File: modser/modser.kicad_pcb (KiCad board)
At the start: 2 copper layers, 32 x 32 mm, 21 parts, among them IC1 AS5600-ASOT, J1 Conn_01x03_Socket, J3 Conn_01x02_Socket, U1 DRV8313PWPR, U2 XIAO-RP2040-DIP, U3 AP63203WU-7

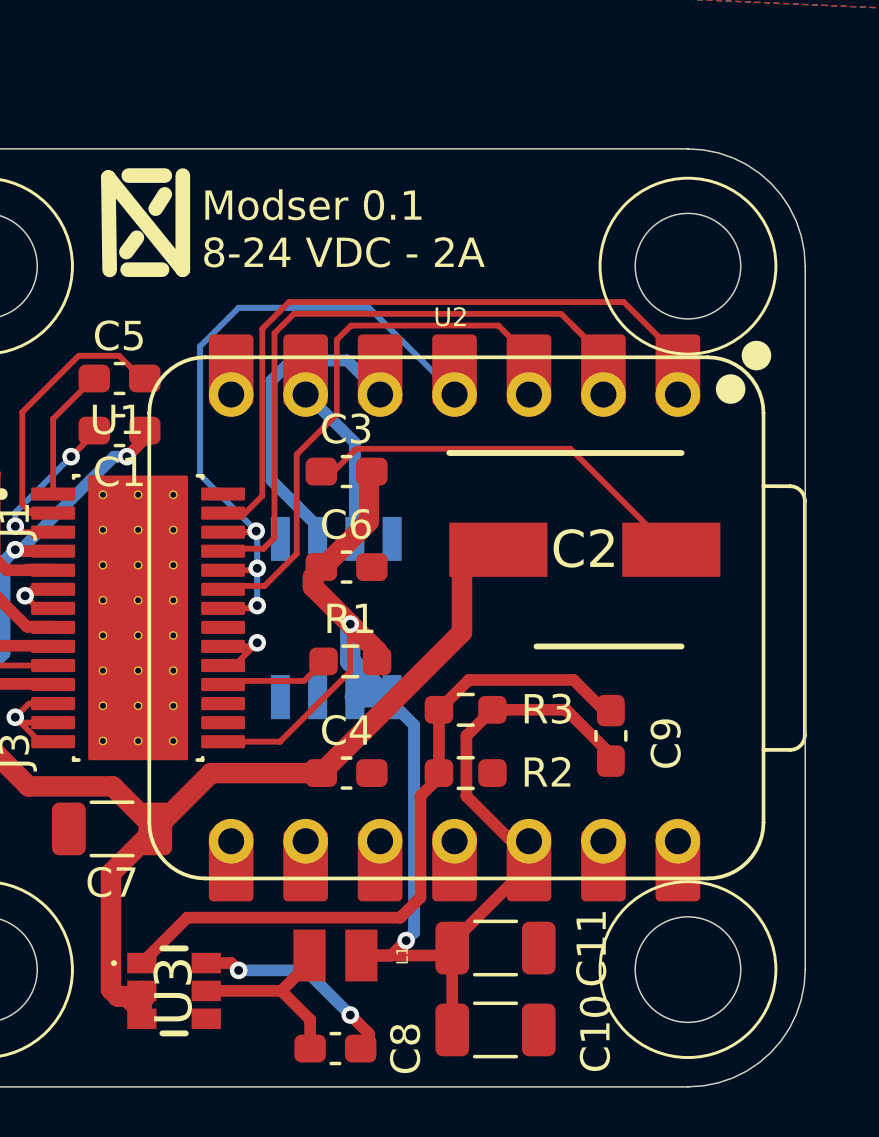
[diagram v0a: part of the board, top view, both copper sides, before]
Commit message: Fixed issue with design around power regulator
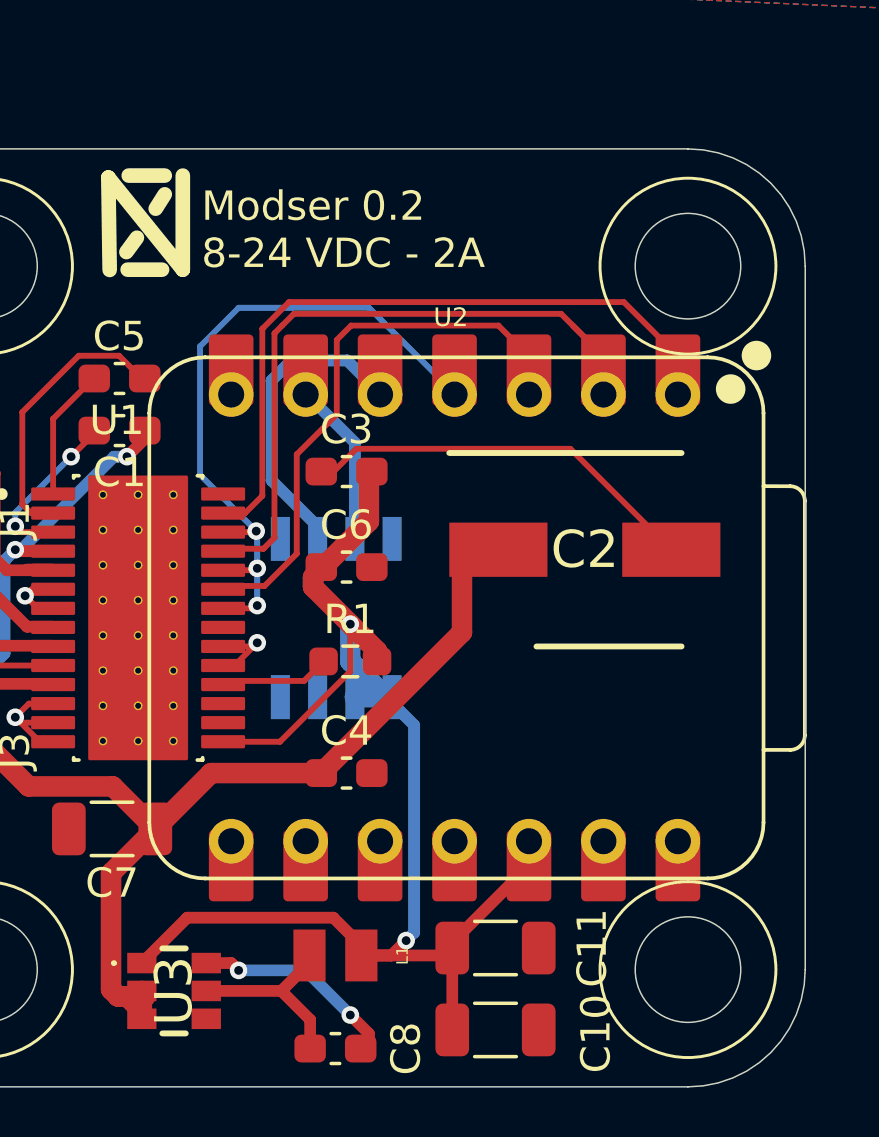
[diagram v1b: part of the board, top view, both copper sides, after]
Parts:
- removed C9: 100 pF, Capacitor_SMD:C_0603_1608Metric_Pad1.08x0.95mm_HandSolder
- removed R2: 30.9 kOhm, Resistor_SMD:R_0603_1608Metric_Pad0.98x0.95mm_HandSolder
- removed R3: 62 kOhm, Resistor_SMD:R_0603_1608Metric_Pad0.98x0.95mm_HandSolder
- L1: value 2.2 uH -> 3.9 uH
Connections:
- U3 pad 1: RegFB -> +3.3V
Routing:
- net RegFB: track 24.0 -> 0.00 mm
- net +3.3V: track 51.2 -> 48.7 mm
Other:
- board text added: "Modser 0.2 8-24 VDC - 2A"
- board text removed: "Modser 0.1 8-24 VDC - 2A"

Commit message: Fixed issue where reset and sleep lines were never pulled high as required
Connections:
- U1 pad 16: unconnected-(U1-~{RESET}-Pad16) -> Enable
- U1 pad 17: unconnected-(U1-~{SLEEP}-Pad17) -> Enable
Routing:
- net Enable: track 23.1 -> 27.6 mm, vias 3 -> 4
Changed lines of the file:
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@@
 	(net 18 "Enable")
 	(net 19 "Net-(U1-IN1)")
-	(net 20 "unconnected-(U1-~{SLEEP}-Pad17)")
-	(net 21 "unconnected-(U1-NC-Pad21)")
-	(net 22 "Net-(U1-IN2)")
-	(net 23 "unconnected-(U1-~{RESET}-Pad16)")
-	(net 24 "unconnected-(U1-EXP-Pad29)")
-	(net 25 "unconnected-(U2-GPIO1{slash}RX-Pad8)")
-	(net 26 "unconnected-(U2-GPIO0{slash}TX-Pad7)")
-	(net 27 "unconnected-(U2-GPIO2{slash}SCK-Pad9)")
-	(net 28 "unconnected-(U2-VBUS-Pad14)")
-	(net 29 "unconnected-(U2-GPIO2{slash}SCK-Pad9)_1")
-	(net 30 "unconnected-(U2-GPIO3{slash}MOSI-Pad11)")
-	(net 31 "unconnected-(U2-GPIO4{slash}MISO-Pad10)")
-	(net 32 "unconnected-(U2-GPIO3{slash}MOSI-Pad11)_1")
-	(net 33 "unconnected-(U2-VBUS-Pad14)_1")
-	(net 34 "unconnected-(U2-GPIO4{slash}MISO-Pad10)_1")
-	(net 35 "unconnected-(U2-GPIO1{slash}RX-Pad8)_1")
-	(net 36 "unconnected-(U2-GPIO0{slash}TX-Pad7)_1")
+	(net 20 "unconnected-(U1-NC-Pad21)")
+	(net 21 "Net-(U1-IN2)")
+	(net 22 "unconnected-(U1-EXP-Pad29)")
+	(net 23 "unconnected-(U2-GPIO1{slash}RX-Pad8)")
+	(net 24 "unconnected-(U2-GPIO0{slash}TX-Pad7)")
+	(net 25 "unconnected-(U2-GPIO2{slash}SCK-Pad9)")
+	(net 26 "unconnected-(U2-VBUS-Pad14)")
+	(net 27 "unconnected-(U2-GPIO2{slash}SCK-Pad9)_1")
+	(net 28 "unconnected-(U2-GPIO3{slash}MOSI-Pad11)")
+	(net 29 "unconnected-(U2-GPIO4{slash}MISO-Pad10)")
+	(net 30 "unconnected-(U2-GPIO3{slash}MOSI-Pad11)_1")
+	(net 31 "unconnected-(U2-VBUS-Pad14)_1")
+	(net 32 "unconnected-(U2-GPIO4{slash}MISO-Pad10)_1")
+	(net 33 "unconnected-(U2-GPIO1{slash}RX-Pad8)_1")
+	(net 34 "unconnected-(U2-GPIO0{slash}TX-Pad7)_1")
 	(footprint "Capacitor_SMD:C_1206_3216Metric"
 		(layer "F.Cu")
@@
 			(layers "F.Cu" "F.Mask")
 			(roundrect_rratio 0.1)
-			(net 22 "Net-(U1-IN2)")
+			(net 21 "Net-(U1-IN2)")
 			(pinfunction "GPIO27/ADC1/A1")
 			(pintype "passive")
@@
 			(layers "*.Cu" "*.Mask")
 			(remove_unused_layers no)
-			(net 22 "Net-(U1-IN2)")
+			(net 21 "Net-(U1-IN2)")
 			(pinfunction "GPIO27/ADC1/A1")
 			(pintype "passive")
@@
 			(layers "F.Cu" "F.Mask")
 			(roundrect_rratio 0.1)
-			(net 36 "unconnected-(U2-GPIO0{slash}TX-Pad7)_1")
+			(net 34 "unconnected-(U2-GPIO0{slash}TX-Pad7)_1")
 			(pinfunction "GPIO0/TX")
 			(pintype "passive+no_connect")
@@
 			(layers "*.Cu" "*.Mask")
 			(remove_unused_layers no)
-			(net 26 "unconnected-(U2-GPIO0{slash}TX-Pad7)")
+			(net 24 "unconnected-(U2-GPIO0{slash}TX-Pad7)")
 			(pinfunction "GPIO0/TX")
 			(pintype "passive+no_connect")
@@
 			(layers "*.Cu" "*.Mask")
 			(remove_unused_layers no)
-			(net 25 "unconnected-(U2-GPIO1{slash}RX-Pad8)")
+			(net 23 "unconnected-(U2-GPIO1{slash}RX-Pad8)")
 			(pinfunction "GPIO1/RX")
 			(pintype "passive+no_connect")
@@
 			(layers "F.Cu" "F.Mask")
 			(roundrect_rratio 0.1)
-			(net 35 "unconnected-(U2-GPIO1{slash}RX-Pad8)_1")
+			(net 33 "unconnected-(U2-GPIO1{slash}RX-Pad8)_1")
 			(pinfunction "GPIO1/RX")
 			(pintype "passive+no_connect")
@@
 			(layers "*.Cu" "*.Mask")
 			(remove_unused_layers no)
-			(net 27 "unconnected-(U2-GPIO2{slash}SCK-Pad9)")
+			(net 25 "unconnected-(U2-GPIO2{slash}SCK-Pad9)")
 			(pinfunction "GPIO2/SCK")
 			(pintype "passive+no_connect")
@@
 			(layers "F.Cu" "F.Mask")
 			(roundrect_rratio 0.1)
-			(net 29 "unconnected-(U2-GPIO2{slash}SCK-Pad9)_1")
+			(net 27 "unconnected-(U2-GPIO2{slash}SCK-Pad9)_1")
 			(pinfunction "GPIO2/SCK")
 			(pintype "passive+no_connect")
@@
 			(layers "*.Cu" "*.Mask")
 			(remove_unused_layers no)
-			(net 34 "unconnected-(U2-GPIO4{slash}MISO-Pad10)_1")
+			(net 32 "unconnected-(U2-GPIO4{slash}MISO-Pad10)_1")
 			(pinfunction "GPIO4/MISO")
 			(pintype "passive+no_connect")
@@
 			(layers "F.Cu" "F.Mask")
 			(roundrect_rratio 0.1)
-			(net 31 "unconnected-(U2-GPIO4{slash}MISO-Pad10)")
+			(net 29 "unconnected-(U2-GPIO4{slash}MISO-Pad10)")
 			(pinfunction "GPIO4/MISO")
 			(pintype "passive+no_connect")
@@
 			(layers "*.Cu" "*.Mask")
 			(remove_unused_layers no)
-			(net 30 "unconnected-(U2-GPIO3{slash}MOSI-Pad11)")
+			(net 28 "unconnected-(U2-GPIO3{slash}MOSI-Pad11)")
 			(pinfunction "GPIO3/MOSI")
 			(pintype "passive+no_connect")
@@
 			(layers "F.Cu" "F.Mask")
 			(roundrect_rratio 0.1)
-			(net 32 "unconnected-(U2-GPIO3{slash}MOSI-Pad11)_1")
+			(net 30 "unconnected-(U2-GPIO3{slash}MOSI-Pad11)_1")
 			(pinfunction "GPIO3/MOSI")
 			(pintype "passive+no_connect")
@@
 			(layers "*.Cu" "*.Mask")
 			(remove_unused_layers no)
-			(net 28 "unconnected-(U2-VBUS-Pad14)")
+			(net 26 "unconnected-(U2-VBUS-Pad14)")
 			(pinfunction "VBUS")
 			(pintype "passive+no_connect")
@@
 			(layers "F.Cu" "F.Mask")
 			(roundrect_rratio 0.1)
-			(net 33 "unconnected-(U2-VBUS-Pad14)_1")
+			(net 31 "unconnected-(U2-VBUS-Pad14)_1")
 			(pinfunction "VBUS")
 			(pintype "passive+no_connect")
@@
 			(layers "F.Cu" "F.Paste")
 			(roundrect_rratio 0.1)
-			(net 23 "unconnected-(U1-~{RESET}-Pad16)")
+			(net 18 "Enable")
 			(pinfunction "~{RESET}")
-			(pintype "input+no_connect")
+			(pintype "input")
 		)
 		(pad "17" smd roundrect
@@
 			(layers "F.Cu" "F.Paste")
 			(roundrect_rratio 0.1)
-			(net 20 "unconnected-(U1-~{SLEEP}-Pad17)")
+			(net 18 "Enable")
 			(pinfunction "~{SLEEP}")
-			(pintype "input+no_connect")
+			(pintype "input")
 		)
 		(pad "18" smd roundrect
@@
 			(layers "F.Cu" "F.Paste")
 			(roundrect_rratio 0.1)
-			(net 21 "unconnected-(U1-NC-Pad21)")
+			(net 20 "unconnected-(U1-NC-Pad21)")
 			(pinfunction "NC")
 			(pintype "no_connect")
@@
 			(layers "F.Cu" "F.Paste")
 			(roundrect_rratio 0.1)
-			(net 22 "Net-(U1-IN2)")
+			(net 21 "Net-(U1-IN2)")
 			(pinfunction "IN2")
 			(pintype "input")
@@
 			(size 0.1 0.1)
 			(layers "F.Cu")
-			(net 24 "unconnected-(U1-EXP-Pad29)")
+			(net 22 "unconnected-(U1-EXP-Pad29)")
 			(pinfunction "EXP")
 			(pintype "power_in+no_connect")
@@
 		(net 18)
 	)
+	(segment
+		(start 89.641 72)
+		(end 89.641 72.575)
+		(width 0.2)
+		(layer "F.Cu")
+		(net 18)
+	)
+	(via
+		(at 89.641 72)
+		(size 0.6)
+		(drill 0.3)
+		(layers "F.Cu" "B.Cu")
+		(net 18)
+	)
 	(via
 		(at 90.769998 66.04)
@@
 	)
 	(segment
+		(start 89.641 69.744)
+		(end 89.641 72)
+		(width 0.2)
+		(layer "B.Cu")
+		(net 18)
+	)
+	(segment
 		(start 88.853 59.737)
 		(end 90.17 58.42)
@@
 	)
 	(segment
+		(start 90.805 68.58)
+		(end 89.641 69.744)
+		(width 0.2)
+		(layer "B.Cu")
+		(net 18)
+	)
+	(segment
 		(start 89.641 65.425)
 		(end 90.390999 65.425)
@@
 		(width 0.2)
 		(layer "F.Cu")
-		(net 22)
+		(net 21)
 	)
 	(segment
@@
 		(width 0.2)
 		(layer "F.Cu")
-		(net 22)
+		(net 21)
 	)
 	(segment
@@
 		(width 0.2)
 		(layer "F.Cu")
-		(net 22)
+		(net 21)
 	)
 	(segment
@@
 		(width 0.2)
 		(layer "F.Cu")
-		(net 22)
+		(net 21)
 	)
 	(segment
@@
 		(width 0.2)
 		(layer "F.Cu")
-		(net 22)
+		(net 21)
 	)
 	(segment
@@
 		(width 0.2)
 		(layer "F.Cu")
-		(net 22)
+		(net 21)
 	)
 	(segment
@@
 		(width 0.2)
 		(layer "F.Cu")
-		(net 22)
+		(net 21)
 	)
 	(segment
@@
 		(width 0.2)
 		(layer "F.Cu")
-		(net 22)
+		(net 21)
 	)
 	(segment
@@
 		(width 0.2)
 		(layer "F.Cu")
-		(net 22)
+		(net 21)
 	)
 	(zone

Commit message: Sent for production
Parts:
- added C12: 22 pf, Capacitor_SMD:C_0603_1608Metric_Pad1.08x0.95mm_HandSolder, F.Cu at (125.0, 81.5)
- added C9: 22 pf, Capacitor_SMD:C_0603_1608Metric_Pad1.08x0.95mm_HandSolder, F.Cu at (125.0, 74.5)
- added J4: Conn_01x02_Socket, Connector_PinHeader_2.54mm:PinHeader_1x02_P2.54mm_Vertical, F.Cu at (123.5, 64.5)
- added JP1: Jumper_2_Open, Jumper:SolderJumper-2_P1.3mm_Bridged_RoundedPad1.0x1.5mm, F.Cu at (120.0, 56.6)
- added R2: 120 Ohm, Resistor_SMD:R_0603_1608Metric_Pad0.98x0.95mm_HandSolder, F.Cu at (116.5, 57.0)
- added R3: 10k Ohm, Resistor_SMD:R_0603_1608Metric_Pad0.98x0.95mm_HandSolder, F.Cu at (112.0, 55.5)
- added R4: 10k Ohm, Resistor_SMD:R_0603_1608Metric_Pad0.98x0.95mm_HandSolder, F.Cu at (111.4, 70.5)
- added U4: MCP2515-I_SO, MCP2515_I_SO:SOIC127P1030X265-18N, F.Cu at (116.0, 78.0)
- added U5: SN65HVD230DR, footprints:D8, F.Cu at (114.4, 64.0)
- added Y1: 8Mhz resonator, NX3225GD_8MHZ_STD_CRA_3:XTAL_NX3225GD-8MHZ-STD-CRA-3_NDK, F.Cu at (125.0, 78.0)
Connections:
- U2 pad 10: unconnected-(U2-GPIO4/MISO-Pad10) -> MISO
- U2 pad 11: unconnected-(U2-GPIO3/MOSI-Pad11)_1 -> MOSI
- U2 pad 8: unconnected-(U2-GPIO1/RX-Pad8)_1 -> CS
- U2 pad 9: unconnected-(U2-GPIO2/SCK-Pad9)_1 -> SCK
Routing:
- net SCK: track 0.00 -> 30.6 mm, vias 0 -> 1
- net CS: track 0.00 -> 25.4 mm
- net Net-(J4-Pin_2): track 0.00 -> 23.4 mm
- net MISO: track 0.00 -> 21.6 mm
- net MOSI: track 0.00 -> 20.8 mm, vias 0 -> 1
- net Net-(U4-RXCAN): track 0.00 -> 17.9 mm, vias 0 -> 2
- net Net-(U4-TXCAN): track 0.00 -> 16.8 mm, vias 0 -> 2
- net Net-(J4-Pin_1): track 0.00 -> 14.4 mm
- net Net-(U4-OSC1): track 0.00 -> 11.6 mm
- net osc2: track 0.00 -> 11.6 mm
- net +3.3V: track 48.7 -> 58.6 mm
- net Net-(U5-RS): track 0.00 -> 6.17 mm
- net GND: track 26.0 -> 31.4 mm, vias 4 -> 6
- net Net-(JP1-A): track 0.00 -> 3.54 mm
- net Net-(U4-~{RESET}): track 0.00 -> 2.95 mm
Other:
- board size 32 x 32 mm -> 51.5 x 32 mm
- board text added: "Modser 0.3 8-24 VDC - 2A"
- board text removed: "Modser 0.2 8-24 VDC - 2A"
